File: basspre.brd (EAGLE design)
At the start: 100 x 80 mm, 23 parts, among them U101 TLE2426IDR, U102 LF351D, U103 LM4250

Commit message: added silkscreen started (rough) sim
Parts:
- added U$1: (no value), SparkFun:OSHW-LOGO-L
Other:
- board size 100 x 80 mm -> 37.5 x 28.7 mm
- board text added: "BASSPRE-MM2 ALPHA"
- board text added: "CC-BY-SA"
- board text added: "github.com/russellmcc"

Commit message: fix up values
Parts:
- C108: value 120pf -> 47nF
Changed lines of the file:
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@@
 <attribute name="VALUE" x="11.938" y="5.969" size="1.27" layer="27" rot="R270"/>
 </element>
-<element name="C108" library="resistor" package="C0603" value="120pf" x="11.43" y="5.08" smashed="yes" rot="R270">
+<element name="C108" library="resistor" package="C0603" value="47nF" x="11.43" y="5.08" smashed="yes" rot="R270">
 <attribute name="NAME" x="12.954" y="2.54" size="0.8128" layer="25" rot="R90"/>
 <attribute name="VALUE" x="9.398" y="5.969" size="1.27" layer="27" rot="R270"/>

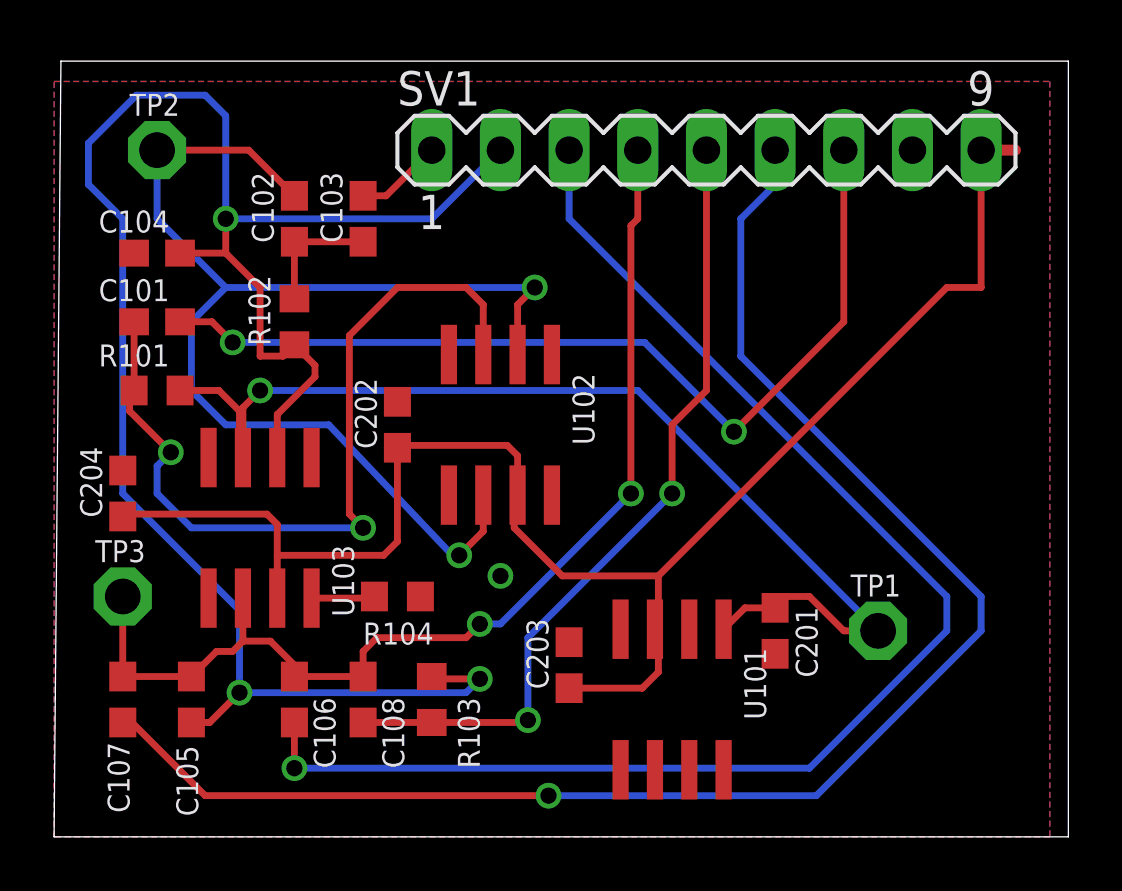
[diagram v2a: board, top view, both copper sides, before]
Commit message: added simulations, changed some values around
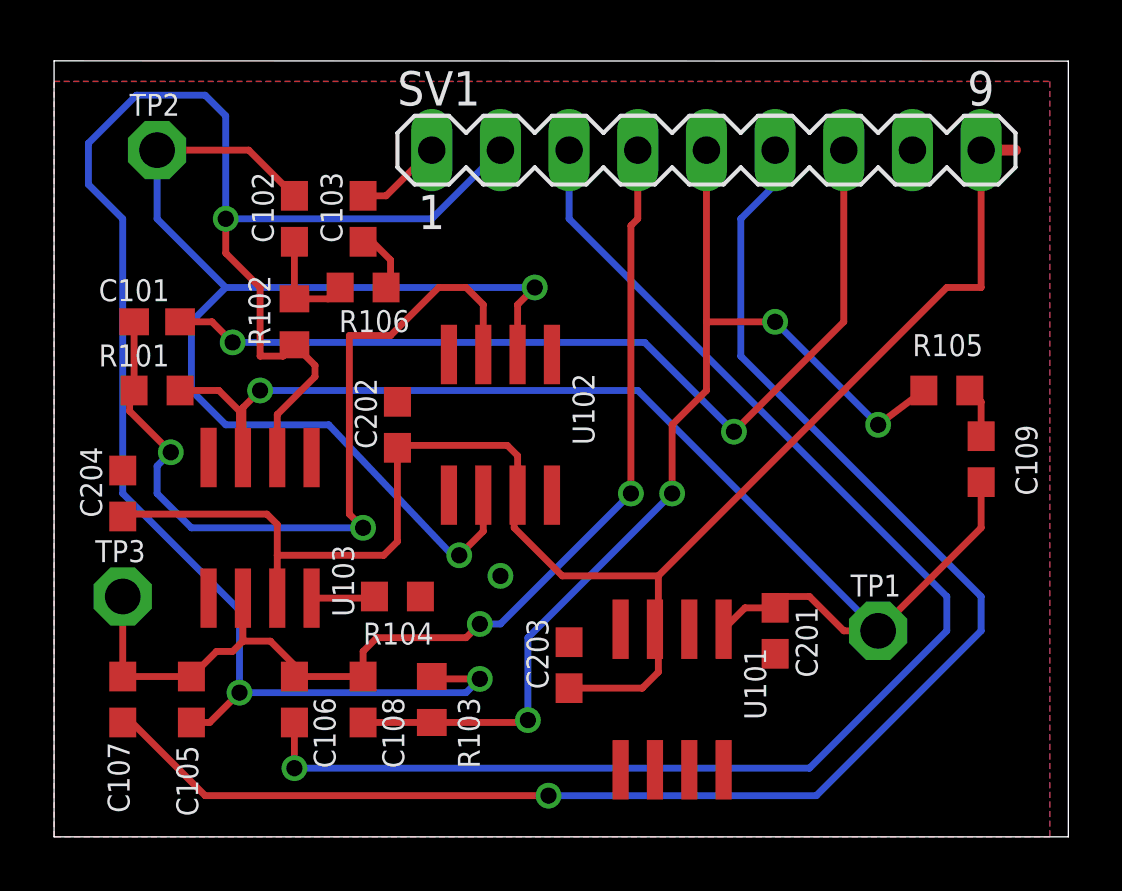
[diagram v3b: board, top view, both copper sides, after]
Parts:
- removed C104: 1uF, resistor:C0603
- added C109: 10uF, resistor:C0603
- added R105: 10K, resistor:R0603
- added R106: 100K, resistor:R0603
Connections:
- new net N$4: C109.1, R105.2
- new net N$5: C103.2, R106.2
- net BASS1: now also R105.1
- net GND: no longer C104.2
- net N$1: now also R106.1; no longer C103.2
- net TREBLE2: no longer C104.1
- net VGND: now also C109.2
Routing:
- net BASS1: track 29.9 -> 40.0 mm, vias 2 -> 4
- net VGND: track 40.3 -> 47.4 mm
- net N$5: track 0.00 -> 2.38 mm
- net N$4: track 0.00 -> 1.86 mm
- net TREBLE2: track 70.7 -> 69.1 mm
- net N$1: track 4.65 -> 3.97 mm
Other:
- outline, holes or cut-outs redrawn
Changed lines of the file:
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@@
 <wire x1="0" y1="0" x2="37.516" y2="0" width="0" layer="20"/>
 <wire x1="37.516" y1="0" x2="37.516" y2="28.692" width="0" layer="20"/>
-<wire x1="37.516" y1="28.692" x2="0.254" y2="28.692" width="0" layer="20"/>
-<wire x1="0.254" y1="28.692" x2="0" y2="0" width="0" layer="20"/>
+<wire x1="37.516" y1="28.692" x2="0" y2="28.702" width="0" layer="20"/>
+<wire x1="0" y1="28.702" x2="0" y2="0" width="0" layer="20"/>
 <text x="35.56" y="17.78" size="1.6764" layer="22" font="vector" rot="MR0">BASSPRE-MM2
 ALPHA</text>
@@
 <attribute name="VALUE" x="2.921" y="14.478" size="1.27" layer="27"/>
 </element>
-<element name="C104" library="resistor" package="C0603" value="1uF" x="3.81" y="21.59" smashed="yes" rot="R180">
-<attribute name="NAME" x="1.651" y="22.352" size="0.8128" layer="25"/>
-<attribute name="VALUE" x="4.699" y="23.622" size="1.27" layer="27" rot="R180"/>
-</element>
 <element name="C105" library="resistor" package="C0603" value="120pf" x="5.08" y="5.08" smashed="yes" rot="R270">
 <attribute name="NAME" x="5.334" y="0.762" size="0.8128" layer="25" rot="R90"/>
@@
 </element>
 <element name="U$1" library="SparkFun" package="OSHW-LOGO-L" value="" x="32.766" y="12.7" rot="MR0"/>
+<element name="R105" library="resistor" package="R0603" value="10K" x="33.02" y="16.51" smashed="yes">
+<attribute name="NAME" x="31.75" y="17.78" size="0.8128" layer="25"/>
+<attribute name="VALUE" x="32.131" y="14.478" size="1.27" layer="27"/>
+</element>
+<element name="C109" library="resistor" package="C0603" value="10uF" x="34.29" y="13.97" smashed="yes" rot="R270">
+<attribute name="NAME" x="35.56" y="15.24" size="0.8128" layer="25" rot="R270"/>
+<attribute name="VALUE" x="32.258" y="14.859" size="1.27" layer="27" rot="R270"/>
+</element>
+<element name="R106" library="resistor" package="R0603" value="100K" x="11.43" y="20.32" smashed="yes">
+<attribute name="NAME" x="10.541" y="18.669" size="0.8128" layer="25"/>
+<attribute name="VALUE" x="10.541" y="18.288" size="1.27" layer="27"/>
+</element>
 </elements>
 <signals>
@@
 <contactref element="U102" pad="4"/>
 <contactref element="U103" pad="4"/>
-<contactref element="C104" pad="2"/>
 <contactref element="SV1" pad="8"/>
 <contactref element="C204" pad="2"/>
@@
 <wire x1="7.62" y1="16.51" x2="21.59" y2="16.51" width="0.254" layer="16"/>
 <wire x1="21.59" y1="16.51" x2="30.48" y2="7.62" width="0.254" layer="16"/>
+<contactref element="C109" pad="2"/>
+<wire x1="34.29" y1="13.12" x2="34.29" y2="11.43" width="0.254" layer="1"/>
+<wire x1="34.29" y1="11.43" x2="30.48" y2="7.62" width="0.254" layer="1"/>
 </signal>
 <signal name="N$3">
@@
 <wire x1="15.875" y1="17.84" x2="15.875" y2="19.685" width="0.254" layer="1"/>
 <wire x1="15.875" y1="19.685" x2="15.24" y2="20.32" width="0.254" layer="1"/>
-<wire x1="15.24" y1="20.32" x2="12.7" y2="20.32" width="0.254" layer="1"/>
-<wire x1="12.7" y1="20.32" x2="10.922" y2="18.542" width="0.254" layer="1"/>
 <wire x1="10.922" y1="18.542" x2="10.922" y2="11.938" width="0.254" layer="1"/>
 <wire x1="10.922" y1="11.938" x2="11.43" y2="11.43" width="0.254" layer="1"/>
@@
 <wire x1="2.794" y1="15.748" x2="2.794" y2="16.344" width="0.254" layer="1"/>
 <wire x1="2.794" y1="16.344" x2="2.96" y2="16.51" width="0.254" layer="1"/>
+<wire x1="10.922" y1="18.542" x2="12.446" y2="18.542" width="0.254" layer="1"/>
+<wire x1="12.446" y1="18.542" x2="14.224" y2="20.32" width="0.254" layer="1"/>
+<wire x1="14.224" y1="20.32" x2="15.24" y2="20.32" width="0.254" layer="1"/>
 </signal>
 <signal name="INPUT">
@@
 <signal name="TREBLE2">
 <contactref element="U103" pad="2"/>
-<contactref element="C104" pad="1"/>
 <contactref element="C105" pad="2"/>
 <contactref element="R103" pad="1"/>
@@
 <wire x1="15.748" y1="5.842" x2="14.058" y2="5.842" width="0.254" layer="1"/>
 <wire x1="14.058" y1="5.842" x2="13.97" y2="5.93" width="0.254" layer="1"/>
-<wire x1="4.66" y1="21.59" x2="6.35" y2="21.59" width="0.254" layer="1"/>
 <wire x1="7.62" y1="20.32" x2="7.62" y2="17.78" width="0.254" layer="1"/>
 <wire x1="7.62" y1="17.78" x2="8.47" y2="17.78" width="0.254" layer="1"/>
@@
 <wire x1="22.86" y1="12.7" x2="22.86" y2="15.24" width="0.254" layer="1"/>
 <wire x1="22.86" y1="15.24" x2="24.13" y2="16.51" width="0.254" layer="1"/>
-<wire x1="24.13" y1="16.51" x2="24.13" y2="25.4" width="0.254" layer="1"/>
+<wire x1="24.13" y1="16.51" x2="24.13" y2="19.05" width="0.254" layer="1"/>
+<contactref element="R105" pad="1"/>
+<wire x1="24.13" y1="19.05" x2="24.13" y2="25.4" width="0.254" layer="1"/>
+<wire x1="32.17" y1="16.51" x2="30.48" y2="15.24" width="0.254" layer="1"/>
+<via x="30.48" y="15.24" extent="1-16" drill="0.6" shape="square"/>
+<wire x1="30.48" y1="15.24" x2="26.67" y2="19.05" width="0.254" layer="16"/>
+<via x="26.67" y="19.05" extent="1-16" drill="0.6" shape="square"/>
+<wire x1="26.67" y1="19.05" x2="24.13" y2="19.05" width="0.254" layer="1"/>
 </signal>
 <signal name="N$1">
 <contactref element="C102" pad="1"/>
 <contactref element="R102" pad="2"/>
-<contactref element="C103" pad="2"/>
-<wire x1="8.89" y1="22.01" x2="11.43" y2="22.01" width="0.254" layer="1"/>
 <wire x1="8.89" y1="22.01" x2="8.89" y2="19.9" width="0.254" layer="1"/>
+<contactref element="R106" pad="1"/>
+<wire x1="8.89" y1="19.9" x2="10.16" y2="19.9" width="0.254" layer="1"/>
+<wire x1="10.16" y1="19.9" x2="10.58" y2="20.32" width="0.254" layer="1"/>
 </signal>
 <signal name="TREBLE3">
@@
 <wire x1="26.67" y1="24.13" x2="26.67" y2="25.4" width="0.254" layer="16"/>
 </signal>
+<signal name="N$4">
+<contactref element="C109" pad="1"/>
+<contactref element="R105" pad="2"/>
+<wire x1="34.29" y1="14.82" x2="34.29" y2="16.09" width="0.254" layer="1"/>
+<wire x1="34.29" y1="16.09" x2="33.87" y2="16.51" width="0.254" layer="1"/>
+</signal>
+<signal name="N$5">
+<contactref element="C103" pad="2"/>
+<contactref element="R106" pad="2"/>
+<wire x1="11.43" y1="22.01" x2="11.772" y2="22.01" width="0.254" layer="1"/>
+<wire x1="11.772" y1="22.01" x2="12.446" y2="21.336" width="0.254" layer="1"/>
+<wire x1="12.446" y1="21.336" x2="12.446" y2="20.486" width="0.254" layer="1"/>
+<wire x1="12.446" y1="20.486" x2="12.28" y2="20.32" width="0.254" layer="1"/>
+</signal>
 </signals>
